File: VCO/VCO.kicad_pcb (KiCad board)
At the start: 2 copper layers, 50 x 200 mm, 87 parts, among them J101 EuroPower, J102 CV, J103 Square, J104 PWM, J105 CV PWM, J106 Triangle, J107 Ramp, Q201 BC547, Q401 DMMT3904, Q501 BC547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

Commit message: Layout VCO done
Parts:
- R501: footprint Resistor_THT:R_Axial_DIN0204_L3.6mm_D1.6mm_P7.62mm_Horizontal -> Resistor_THT:R_Axial_DIN0204_L3.6mm_D1.6mm_P2.54mm_Vertical
- moved R501 48.0 mm to (41.0, 60.1)
- moved R510 43.9 mm to (46.1, 70.9)
- moved R511 43.1 mm to (48.6, 47.2)
- moved Q502 42.6 mm to (57.0, 59.9), turned to 270 degrees
- moved Q501 40.2 mm to (57.0, 67.1), turned to 270 degrees
- moved R506 34.8 mm to (53.8, 56.9), turned to 90 degrees
- moved R508 32.9 mm to (53.7, 68.7), turned to 180 degrees
- moved R512 32.1 mm to (58.2, 56.9), turned to 90 degrees
- moved R502 31.6 mm to (40.5, 49.3), turned to 270 degrees
- moved R509 25.1 mm to (53.8, 63.2), turned to 180 degrees
- moved R503 22.4 mm to (53.7, 66.5), turned to 180 degrees
- moved R507 22.3 mm to (53.7, 73.1), turned to 180 degrees
- moved R505 20.4 mm to (56.0, 56.9), turned to 90 degrees
- moved R504 16.6 mm to (53.8, 60.0), turned to 180 degrees
- moved U502 14.6 mm to (49.2, 83.3)
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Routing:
- net -12V: track 46.7 -> 267.7 mm, vias 0 -> 4
- net +12V: track 75.7 -> 260.7 mm, vias 2 -> 8
- net /Triangle: track 136.0 -> 217.0 mm
- net /Square: track 136.4 -> 210.9 mm, vias 5 -> 4
- net /CVP: track 0.00 -> 43.3 mm
- net /PWM_Level: track 0.00 -> 42.9 mm
- net Net-(R307-Pad2): track 0.00 -> 39.4 mm
- net /Ramp: track 125.6 -> 161.2 mm
- net Net-(R306-Pad1): track 0.00 -> 28.5 mm
- net /Offset: track 0.00 -> 27.7 mm
- net /Sheet5FAD0DD2/~Triangle: track 0.00 -> 21.3 mm
- net Net-(R301-Pad1): track 0.00 -> 18.0 mm
- net /Sheet5FAD0DD2/~Square: track 0.00 -> 15.8 mm
- net Net-(Q501-Pad1): track 0.00 -> 15.7 mm
- net Net-(R511-Pad1): track 0.00 -> 14.2 mm
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- added copper zone on F.Cu, net GND
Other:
- outline, holes or cut-outs redrawn
- board text added: "O"
- board text added: "gain"
- board text added: "offset"
- board text removed: "~Triangle~ & PWM generation"

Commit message: VCO artwork done
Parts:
- moved C401 14.3 mm to (18.0, 72.6), turned to 90 degrees
- moved R404 13.5 mm to (16.0, 86.3)
- moved U401 10.7 mm to (18.7, 83.6), turned to 90 degrees
- moved C402 9.88 mm to (25.3, 86.3), turned to 180 degrees
- moved C404 7.71 mm to (18.7, 88.9), turned to 0 degrees
- moved C403 6.68 mm to (20.2, 72.8), turned to 0 degrees
- moved R401 5.10 mm to (30.7, 70.1)
- moved R303 3.81 mm to (13.8, 82.8)
- moved R402 2.04 mm to (21.2, 86.2)
- moved R403 1.19 mm to (19.4, 67.4)
- moved R304 1.00 mm to (16.6, 105.8)
- moved R103 0.81 mm to (18.8, 108.0)
- moved R102 0.80 mm to (31.3, 112.0)
- moved R302 0.80 mm to (14.0, 105.8)
- moved R305 0.80 mm to (20.2, 105.8)
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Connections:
- U401 pad 1: Net-(C403-Pad1) -> Net-(C404-Pad1)
- U401 pad 2: Net-(C403-Pad2) -> Net-(C404-Pad2)
- U401 pad 6: Net-(C404-Pad2) -> Net-(C403-Pad2)
- U401 pad 7: Net-(C404-Pad1) -> Net-(C403-Pad1)
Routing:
- net +12V: track 260.7 -> 282.2 mm
- net -12V: track 267.7 -> 283.1 mm, vias 4 -> 5
- net Net-(C403-Pad1): track 15.5 -> 28.7 mm
- net /CV: track 12.6 -> 19.7 mm
- net GND: track 19.4 -> 13.0 mm
- net Net-(R301-Pad1): track 18.0 -> 14.2 mm
- net Net-(C403-Pad2): track 16.0 -> 13.9 mm
- net Net-(Q401-Pad4): track 8.55 -> 7.48 mm
- net Net-(R307-Pad2): track 39.4 -> 38.6 mm
- net /CVP: track 43.3 -> 42.5 mm
- net Net-(R306-Pad1): track 28.5 -> 27.7 mm
- net /Offset: track 27.7 -> 26.9 mm
- net Net-(C404-Pad2): track 9.98 -> 9.22 mm
- net /CVoct: track 11.6 -> 12.1 mm
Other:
- board text added: "+/- 1V Reference"
- board text added: "+1V"
- board text added: "-1V"

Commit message: VCO done
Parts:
- removed R303: 0, Resistor_THT:R_Axial_DIN0204_L3.6mm_D1.6mm_P7.62mm_Horizontal
- added R404: 0, Resistor_THT:R_Axial_DIN0204_L3.6mm_D1.6mm_P7.62mm_Horizontal, F.Cu at (13.8, 82.8)
- renumbered R404 to R403, R403 to R405
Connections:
- Q401 pad 2: /CV -> Net-(Q401-Pad2)
- R301 pad 1: Net-(R301-Pad1) -> /CV
- U301 pad 1: Net-(R301-Pad1) -> /CV
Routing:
- net Net-(R301-Pad1): track 14.2 -> 0.00 mm
- net Net-(Q401-Pad2): track 0.00 -> 11.9 mm
- net /CV: track 19.7 -> 31.4 mm

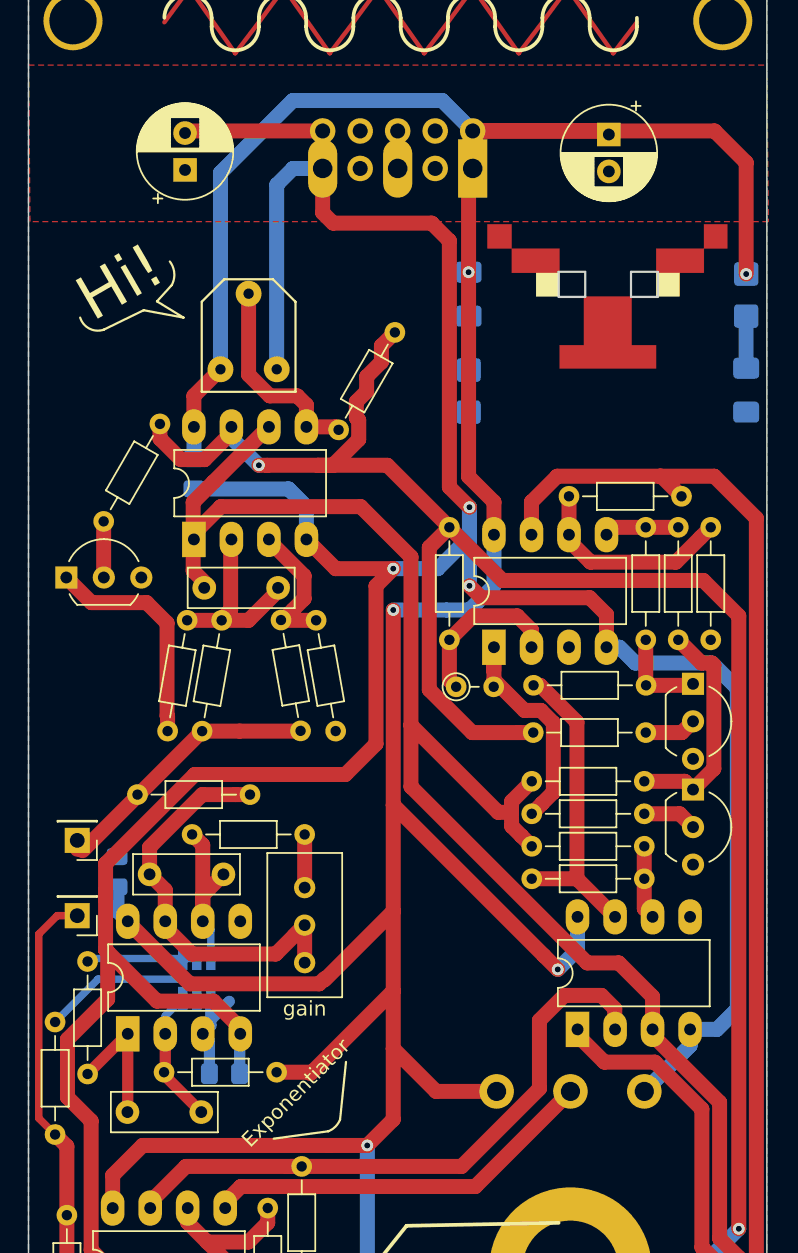
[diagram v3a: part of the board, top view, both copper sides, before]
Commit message: Added HF trim, ready to fab
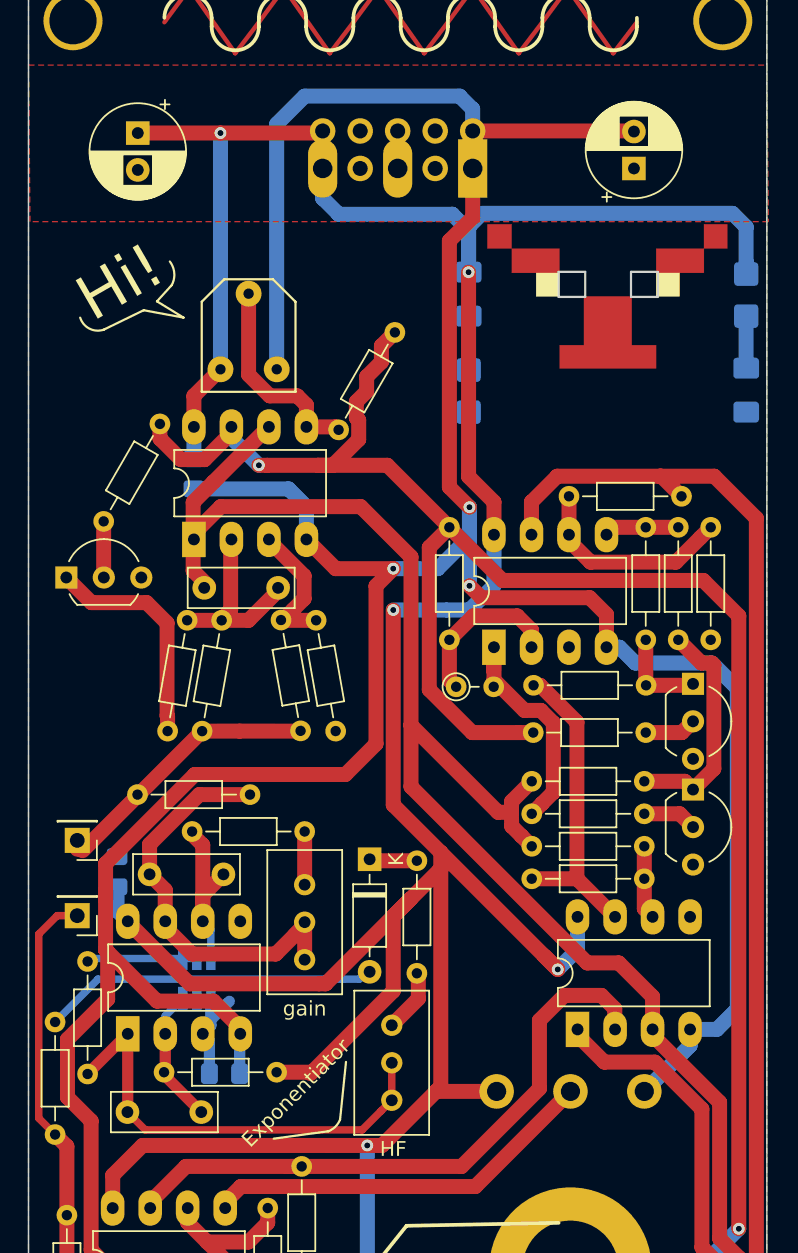
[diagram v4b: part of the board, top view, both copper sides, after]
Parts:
- added D401: 1N4148, Diode_THT:D_DO-35_SOD27_P7.62mm_Horizontal, F.Cu at (35.1, 71.8)
- added R406: 4k7, Resistor_THT:R_Axial_DIN0204_L3.6mm_D1.6mm_P7.62mm_Horizontal, F.Cu at (38.3, 71.9)
- added RV402: 100k, Potentiometer_THT:Potentiometer_Bourns_3296W_Vertical, F.Cu at (36.6, 88.1)
- moved C101 31.9 mm to (19.4, 22.6)
- moved C102 30.4 mm to (53.0, 25.0)
- moved RV401 0.20 mm to (30.7, 73.5)
- moved R401 0.20 mm to (30.7, 69.9)
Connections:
- J101 pad 1: +12V -> -12V
- J101 pad 3: -12V -> +12V
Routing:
- net Net-(C404-Pad1): track 9.25 -> 31.0 mm
- net Net-(D401-Pad2): track 11.9 -> 24.3 mm
- net -12V: track 283.1 -> 294.7 mm
- net Net-(R406-Pad2): track 0.00 -> 4.27 mm
- net Net-(D401-Pad1): track 0.00 -> 3.34 mm
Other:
- board text added: "HF"

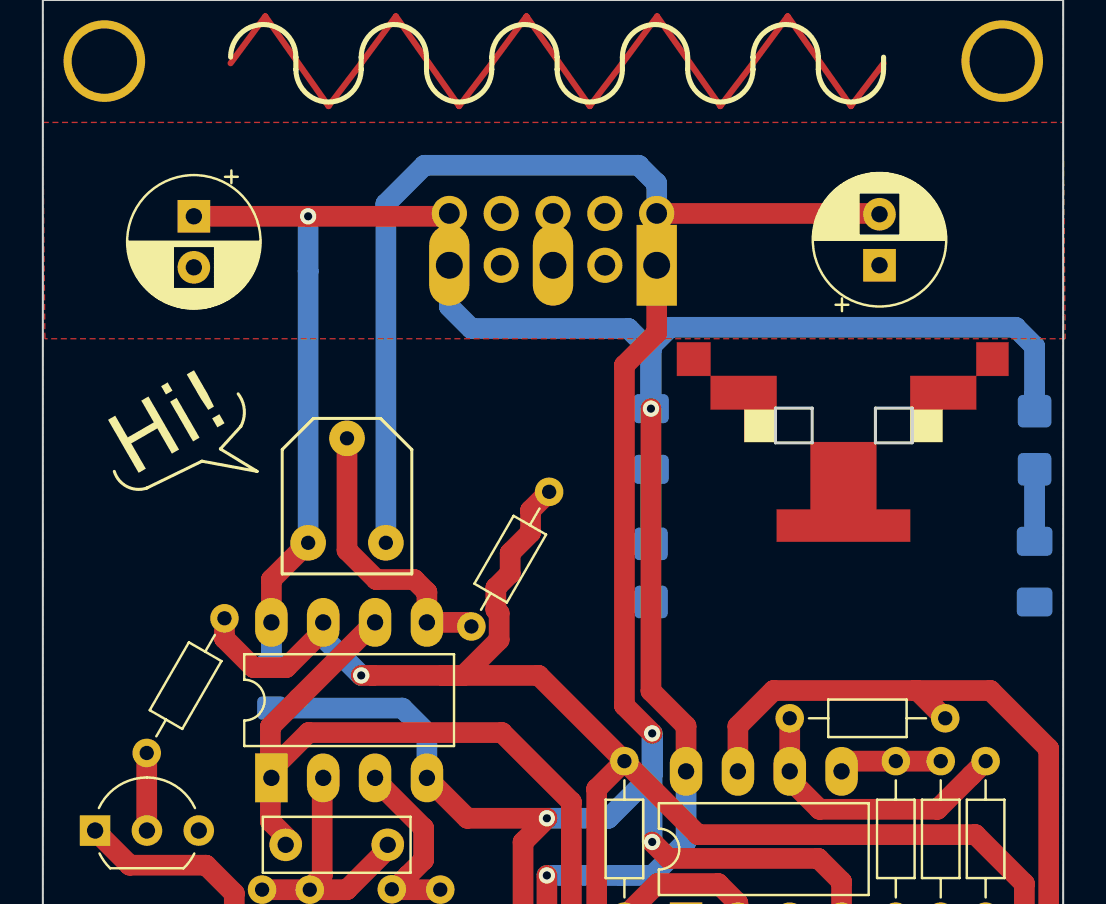
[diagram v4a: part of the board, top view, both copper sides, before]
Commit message: More clearance
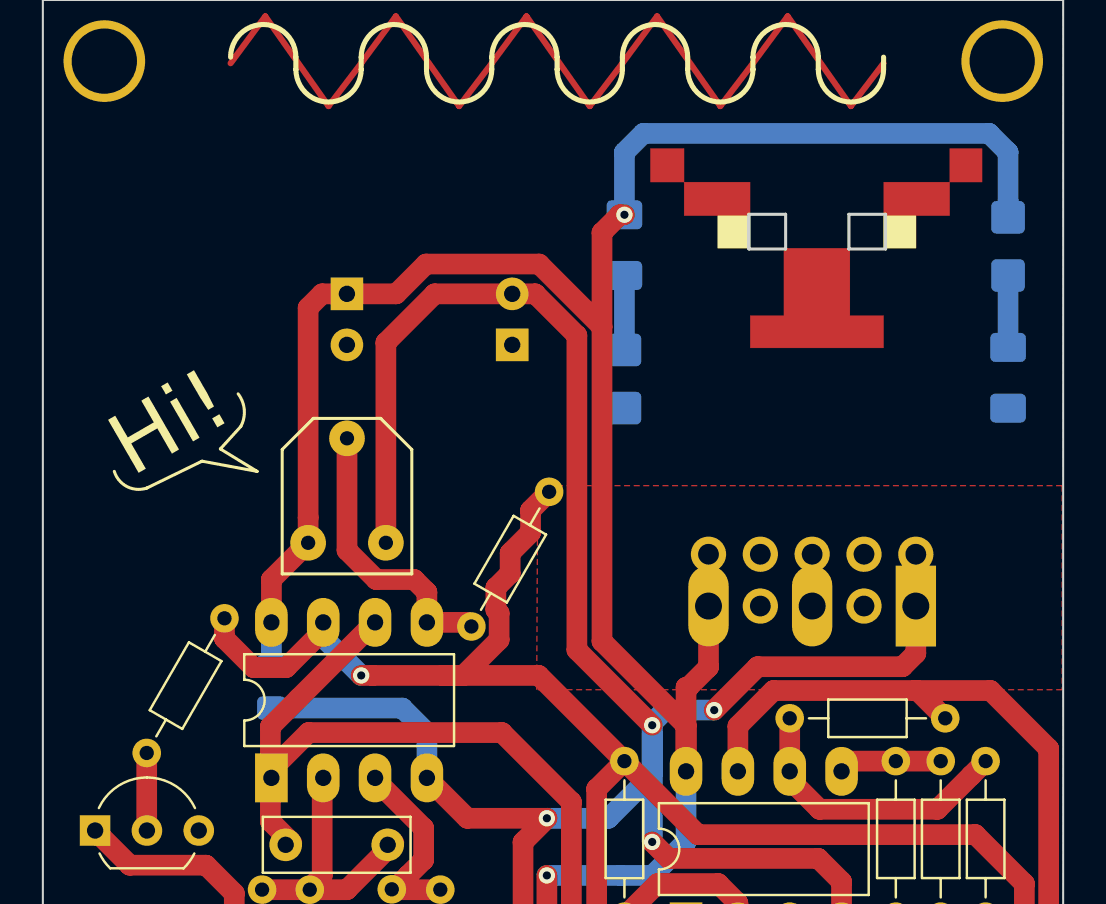
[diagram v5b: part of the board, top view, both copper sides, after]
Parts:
- C101, C102: moved to B.Cu
- moved J101 21.0 mm to (54.8, 41.7)
- moved C102 18.4 mm to (35.0, 28.9)
- moved D102 9.59 mm to (59.3, 24.1)
- moved D103 9.59 mm to (40.5, 30.6)
- moved R111 9.59 mm to (40.5, 24.0)
- moved R114 9.59 mm to (59.3, 30.5)
- moved LOGO101 9.59 mm to (49.9, 27.4)
- moved C101 8.41 mm to (26.9, 26.4)
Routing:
- net -12V: track 294.7 -> 285.5 mm, vias 5 -> 6
- net +12V: track 282.5 -> 286.1 mm, vias 8 -> 7
